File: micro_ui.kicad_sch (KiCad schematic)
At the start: 4 parts

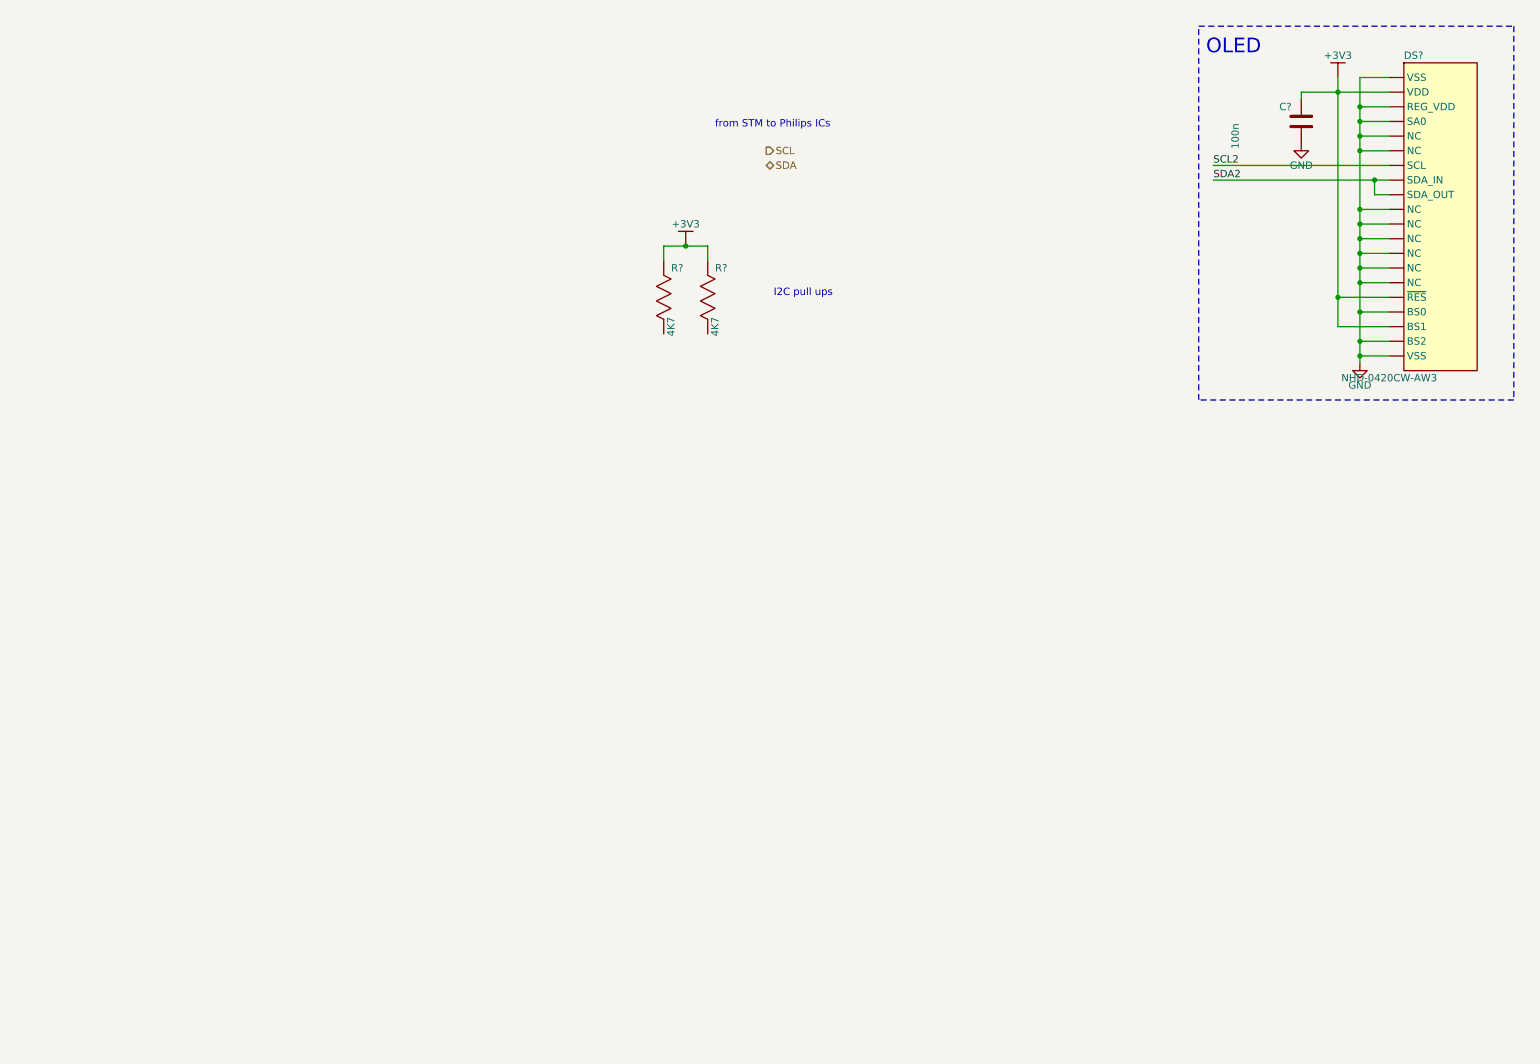
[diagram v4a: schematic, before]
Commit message: continued on schematic, added power sheet
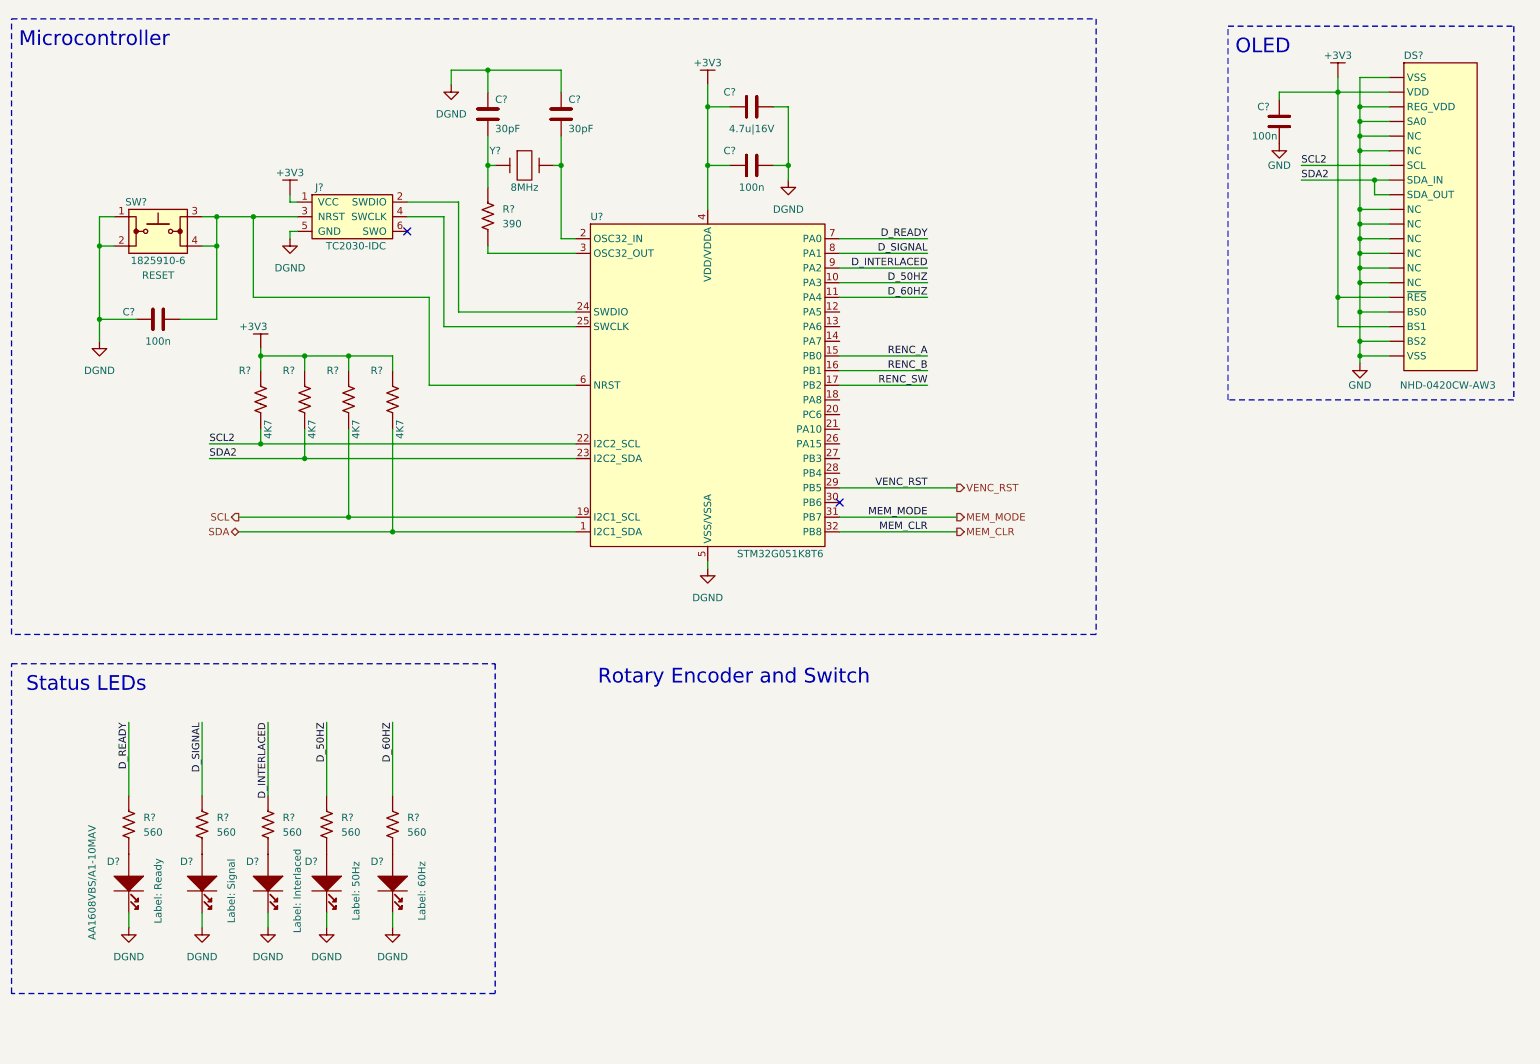
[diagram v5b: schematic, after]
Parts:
- added C? (x2): 100n, symbol tbc:GCJ188R71H104KA12D
- added C?: 4.7u|16V, symbol tbc:GRT188C71C475KE13D
- added C? (x2): 30pF, symbol tbc:GCM1885C2A300GA16D
- added D? (x5): AA1608VBS/A1-10MAV, symbol tbc:AA1608VBS/A1-10MAV
- added J?: TC2030-IDC, symbol tbc:TC2030-IDC
- added R? (x2): 4K7, symbol tbc:RC0603FR-074K7L
- added R? (x5): 560, symbol tbc:RC0603FR-07560RL
- added R?: 390, symbol tbc:RC0603FR-07390RL
- added SW?: 1825910-6, symbol tbc:1825910-6
- added U?: STM32G051K8T6, symbol tbc:STM32G051K8T6
- added Y?: 8MHz, symbol tbc:ECS-80-20-5PX-EM-TR
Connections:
- net +3V3: now also C?.1, C?.1, J?.1 (VCC), R?.2, R?.2, U?.4 (VDD/VDDA)
- net SCL: now also R?.1, U?.19 (PA9)
- net SCL2: now also R?.1, U?.22 (PA11_[PA9])
- net SDA: now also R?.1, U?.1 (PB9)
- net SDA2: now also R?.1, U?.23 (PA12_[PA10])
- new net: C?.2, J?.3 (NRST), SW?.3, SW?.4, U?.6 (PF2-NRST)
- new net: D?.2 (Anode), R?.1 (x5)
- new net: C?.1, U?.2 (PC14-OSC32_IN), Y?.2
- new net: C?.1, R?.2, Y?.1
- new net: J?.2 (SWDIO), U?.24 (PA13)
- new net: J?.4 (SWCLK), U?.25 (PA14-BOOT0)
- new net: R?.1, U?.3 (PC15-OSC32_OUT)
- new net DGND: C?.1, C?.2, C?.2, C?.2, C?.2, D?.1 (Cathode), D?.1 (Cathode), D?.1 (Cathode), D?.1 (Cathode), D?.1 (Cathode), J?.5 (GND), SW?.1, SW?.2, U?.5 (VSS/VSSA)
- new net D_50HZ: R?.2, U?.10 (PA3)
- new net D_60HZ: R?.2, U?.11 (PA4)
- new net D_INTERLACED: R?.2, U?.9 (PA2)
- new net D_READY: R?.2, U?.7 (PA0)
- new net D_SIGNAL: R?.2, U?.8 (PA1)
- new net MEM_CLR: U?.32 (PB8)
- new net MEM_MODE: U?.31 (PB7)
- new net RENC_A: U?.15 (PB0)
- new net RENC_B: U?.16 (PB1)
- new net RENC_SW: U?.17 (PB2)
- new net VENC_RST: U?.29 (PB5)
- no-connect marks 0 -> 2
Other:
- note added: "Microcontroller"
- note added: "Rotary Encoder and Switch"
- note added: "Status LEDs"
- note removed: "I2C pull ups"
- note removed: "from STM to Philips ICs"
- moved on the sheet: C?

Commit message: updates to power, ferrites etc
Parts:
- Y?: value 8MHz -> ECS-80-20-5PX-EM-TR
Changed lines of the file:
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@@
       (effects (font (size 1.27 1.27)))
     )
-    (property "Value" "8MHz" (at 106.68 45.72 0)
+    (property "Value" "ECS-80-20-5PX-EM-TR" (at 106.68 45.72 0)
       (effects (font (size 1.27 1.27)))
     )
@@
     )
     (pin "1")
+    (instances
+      (project "tbc"
+        (path "/9df71e53-7941-4fd3-a17d-93619e4e3e02/5f11175b-e91a-4557-963e-2b2820dad3c4"
+          (reference "#PWR?") (unit 1)
+        )
+      )
+    )
   )
   (symbol (lib_id "tbc:RC0603FR-074K7L") (at 83.82 82.55 90) (unit 1)

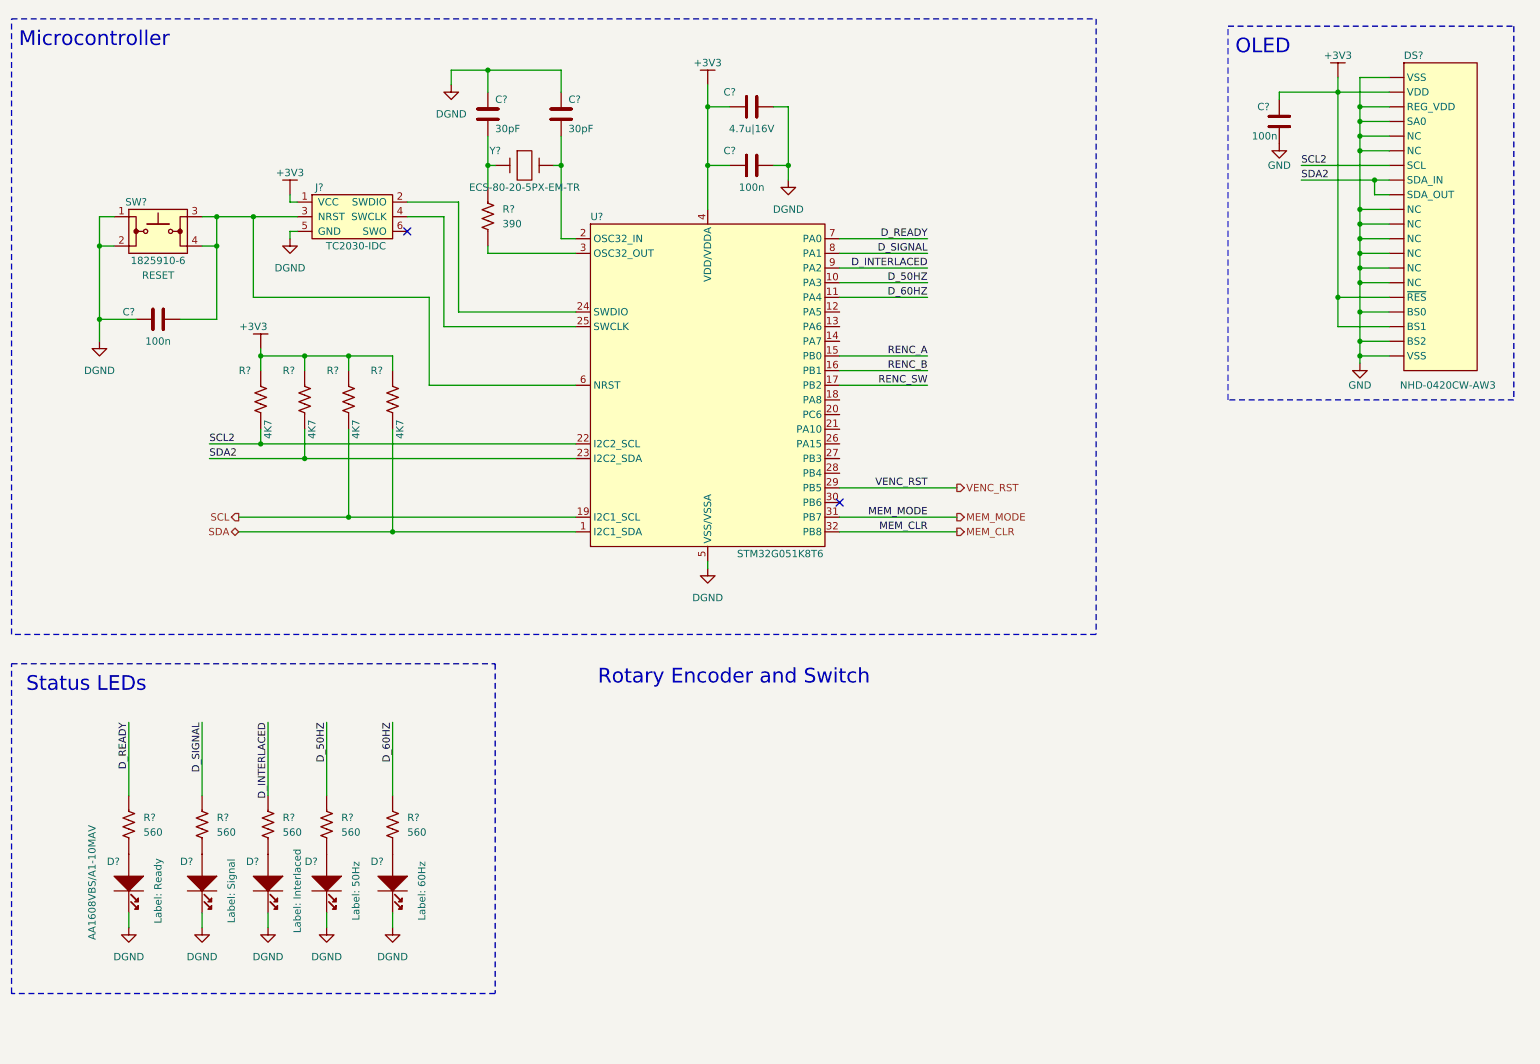
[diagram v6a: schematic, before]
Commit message: added encoder to schematic
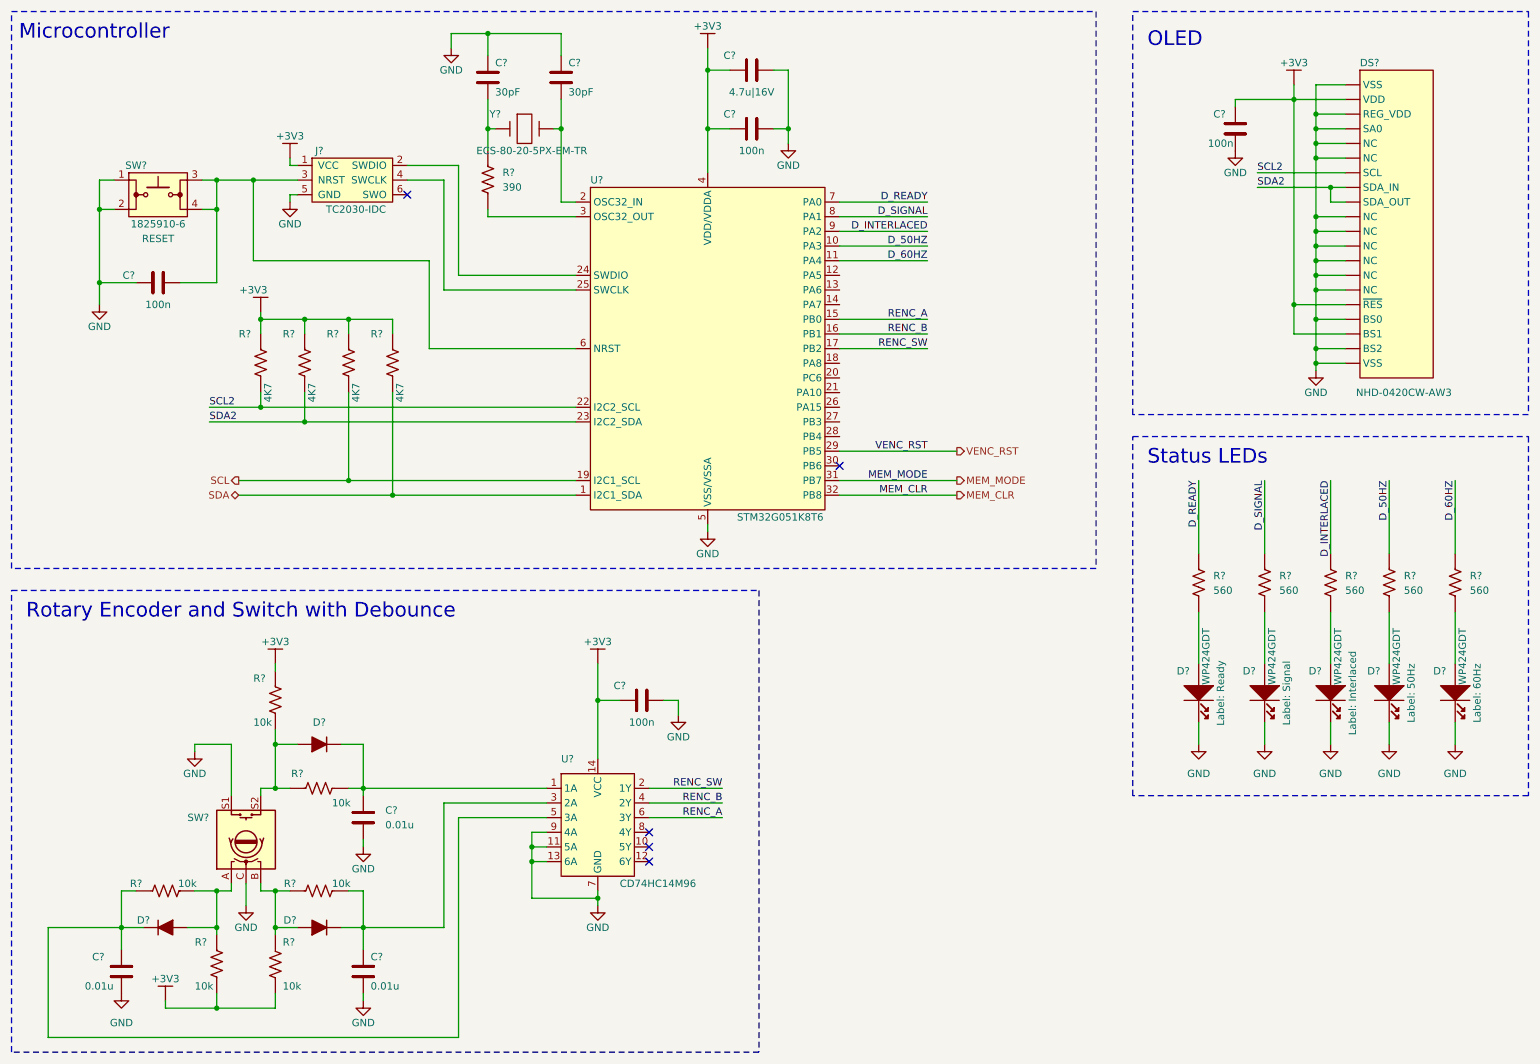
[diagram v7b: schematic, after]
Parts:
- added C? (x3): 0.01u, symbol tbc:GCM188R71H103KA37J
- added C?: 100n, symbol tbc:GCJ188R71H104KA12D
- added D? (x3): 1N4148WS, symbol tbc:1N4148WS
- added R? (x6): 10k, symbol tbc:RC0603FR-0710KL
- added SW?: PEC11R-4220F-S0024, symbol tbc:PEC11R-4220F-S0024
- added U?: CD74HC14M96, symbol tbc:CD74HC14M96
- D? (x5): value AA1608VBS/A1-10MAV -> WP424GDT; symbol tbc:AA1608VBS/A1-10MAV -> tbc:WP424GDT; Mouser 604-AA1608VBSA110M -> 604-WP424GDT
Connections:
- net DGND is gone; now on net GND: C?.1, C?.2, C?.2, C?.2, C?.2, D?.1 (Cathode), D?.1 (Cathode), D?.1 (Cathode), D?.1 (Cathode), D?.1 (Cathode), J?.5 (GND), SW?.1, SW?.2, U?.5 (VSS/VSSA)
- net +3V3: now also C?.1, R?.1, R?.2, R?.2, U?.14 (VCC)
- net GND: now also C?.1, C?.1, C?.1, C?.2, SW?.C, SW?.S1, U?.11 (5A), U?.13 (6A), U?.7 (GND), U?.9 (4A)
- net RENC_A: now also U?.6 (3Y)
- net RENC_B: now also U?.4 (2Y)
- net RENC_SW: now also U?.2 (1Y)
- new net: C?.2, D?.1 (K), R?.1, U?.5 (3A)
- new net: C?.2, D?.1 (K), R?.1, U?.3 (2A)
- new net: D?.2 (A), R?.1, R?.2, SW?.B
- new net: D?.2 (A), R?.2, R?.2, SW?.A
- new net: C?.2, D?.1 (K), R?.1, U?.1 (1A)
- new net: D?.2 (A), R?.1, R?.2, SW?.S2
- no-connect marks 2 -> 5
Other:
- note added: "Rotary Encoder and Switch with Debounce"
- note removed: "Rotary Encoder and Switch"
- moved on the sheet: C?, D?, DS?, J?, R?, SW?, U?, Y?
